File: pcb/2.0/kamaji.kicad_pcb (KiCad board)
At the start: 2 copper layers, 100 x 100 mm, 92 parts, among them J1 RJ10, J2 RJ10, J3 RJ10, J4 RJ10, J5 RJ10, J6 RJ10, J7 USB_B, J8 USB_A, Q1 2N3904, Q2 IRL540N, Q3 IRL540N, SW1 SW_Push, SW2 SW_Push, SW3 SW_Push, U1 ATMEGA32U4-AU, Y1 16MHz

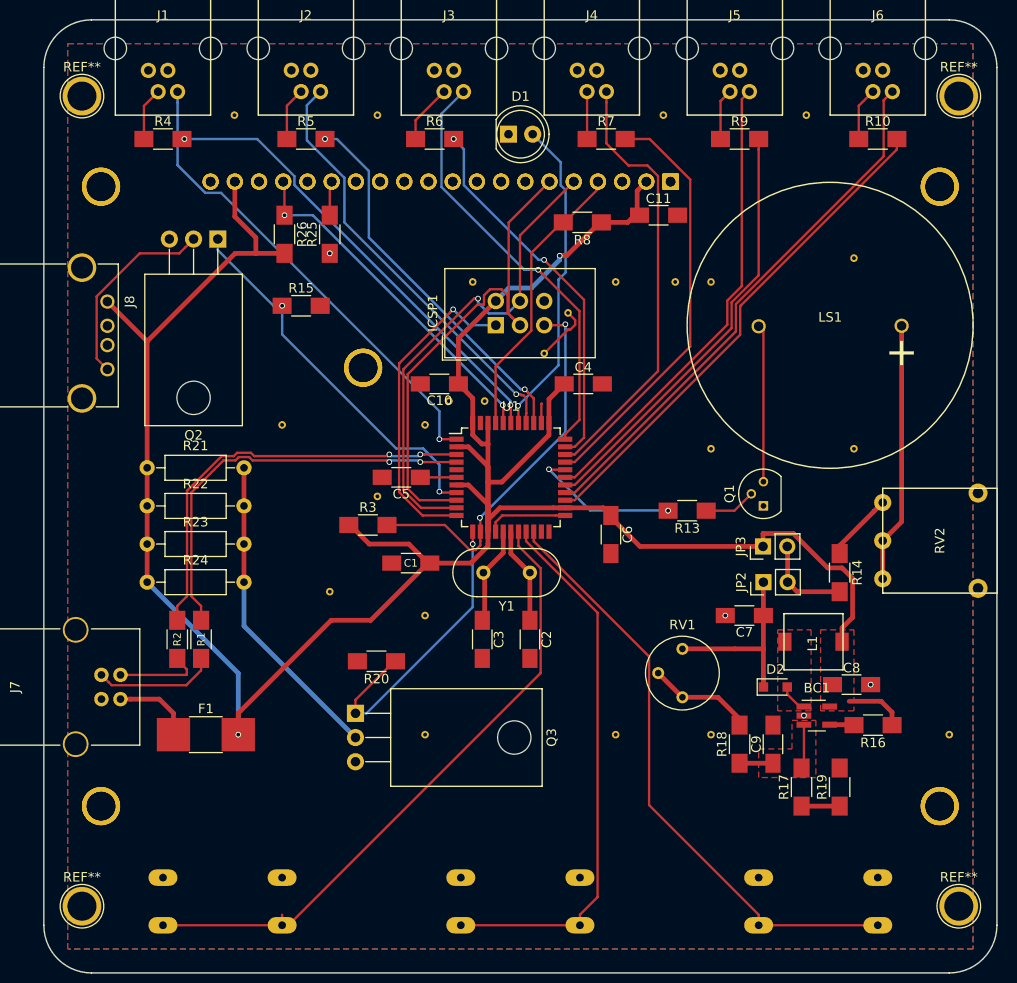
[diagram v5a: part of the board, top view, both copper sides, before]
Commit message: silkscreen text
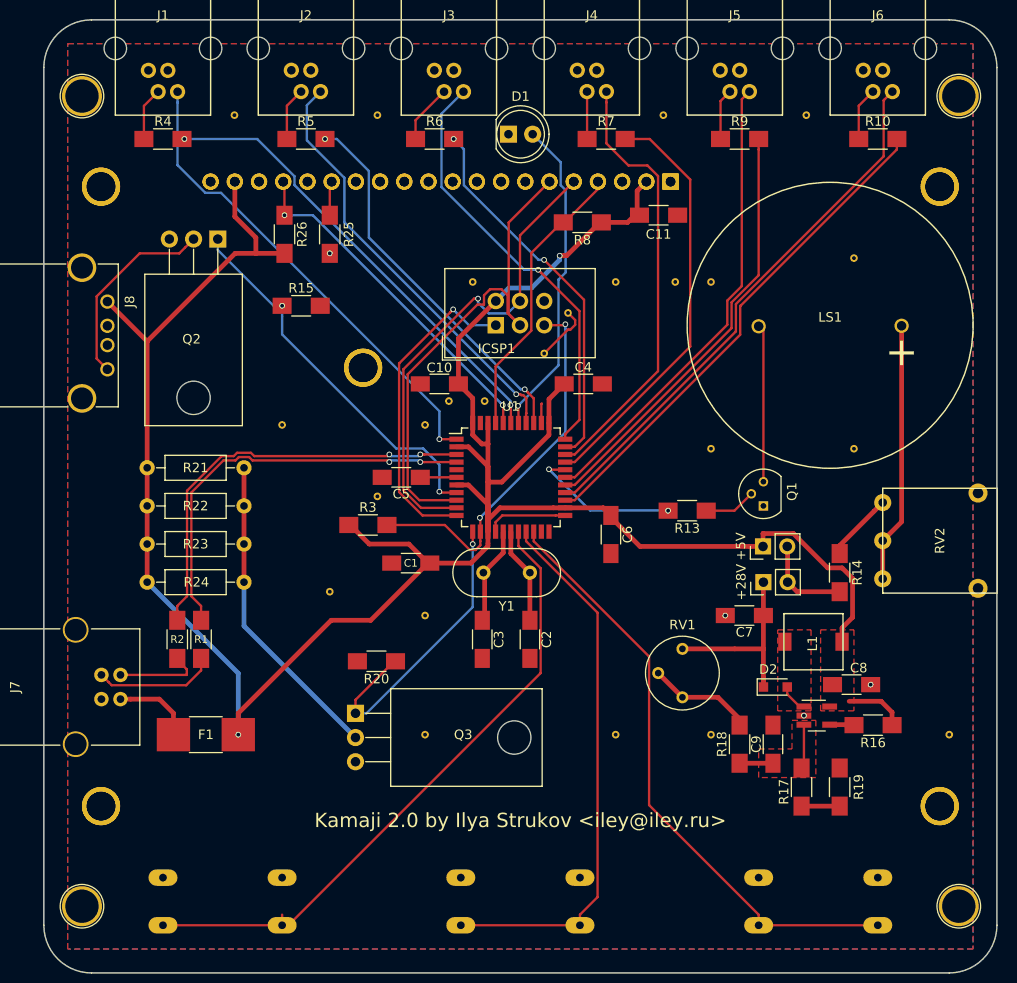
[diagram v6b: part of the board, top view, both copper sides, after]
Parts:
- renumbered JP2 to +28V, JP3 to +5V
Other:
- board text added: "Kamaji 2.0 by Ilya Strukov <iley@iley.ru>"
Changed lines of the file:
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@@
 (kicad_pcb (version 4) (host pcbnew 4.0.7)
   (general
-    (links 0)
+    (links 203)
     (no_connects 1)
     (area 49.924999 49.924999 150.075001 150.075001)
     (thickness 1.6)
-    (drawings 8)
+    (drawings 9)
     (tracks 450)
     (zones 0)
@@
     (mod_text_size 1 1)
     (mod_text_width 0.15)
-    (pad_size 4.064 4.064)
-    (pad_drill 3.048)
+    (pad_size 4.2 4.2)
+    (pad_drill 3.5)
     (pad_to_mask_clearance 0.2)
     (aux_axis_origin 0 0)
@@
     (descr "module 1 pin (ou trou mecanique de percage)")
     (tags DEV)
-    (fp_text reference REF** (at 0 -3.048) (layer F.SilkS)
+    (fp_text reference REF** (at 0 -3.048) (layer F.SilkS) hide
       (effects (font (size 1 1) (thickness 0.15)))
     )
@@
     (fp_circle (center 0 0) (end 2.6 0) (layer F.CrtYd) (width 0.05))
     (fp_circle (center 0 0) (end 0 -2.286) (layer F.SilkS) (width 0.12))
-    (pad "" np_thru_hole circle (at 0 0) (size 4.064 4.064) (drill 3.048) (layers *.Cu *.Mask))
+    (pad "" np_thru_hole circle (at 0 0) (size 4.2 4.2) (drill 3.5) (layers *.Cu *.Mask))
   )
   (module Connectors:1pin (layer F.Cu)
@@
     (descr "module 1 pin (ou trou mecanique de percage)")
     (tags DEV)
-    (fp_text reference REF** (at 0 -3.048) (layer F.SilkS)
+    (fp_text reference REF** (at 0 -3.048) (layer F.SilkS) hide
       (effects (font (size 1 1) (thickness 0.15)))
     )
@@
     (fp_circle (center 0 0) (end 2.6 0) (layer F.CrtYd) (width 0.05))
     (fp_circle (center 0 0) (end 0 -2.286) (layer F.SilkS) (width 0.12))
-    (pad "" np_thru_hole circle (at 0 0) (size 4.064 4.064) (drill 3.048) (layers *.Cu *.Mask))
+    (pad "" np_thru_hole circle (at 0 0) (size 4.2 4.2) (drill 3.5) (layers *.Cu *.Mask))
   )
   (module Connectors:1pin (layer F.Cu)
@@
     (descr "module 1 pin (ou trou mecanique de percage)")
     (tags DEV)
-    (fp_text reference REF** (at 0 -3.048) (layer F.SilkS)
+    (fp_text reference REF** (at 0 -3.048) (layer F.SilkS) hide
       (effects (font (size 1 1) (thickness 0.15)))
     )
@@
     (fp_circle (center 0 0) (end 2.6 0) (layer F.CrtYd) (width 0.05))
     (fp_circle (center 0 0) (end 0 -2.286) (layer F.SilkS) (width 0.12))
-    (pad "" np_thru_hole circle (at 0 0) (size 4.064 4.064) (drill 3.048) (layers *.Cu *.Mask))
+    (pad "" np_thru_hole circle (at 0 0) (size 4.2 4.2) (drill 3.5) (layers *.Cu *.Mask))
   )
   (module kamaji:Via_0.8mm (layer F.Cu)
@@
     (descr "TO-220-3, Horizontal, RM 2.54mm")
     (tags "TO-220-3 Horizontal RM 2.54mm")
-    (fp_text reference Q3 (at 2.54 -20.58 270) (layer F.SilkS)
+    (fp_text reference Q3 (at 2.24 -11.3 360) (layer F.SilkS)
       (effects (font (size 1 1) (thickness 0.15)))
     )
@@
     (descr "TO-92 leads molded, narrow, drill 0.6mm (see NXP sot054_po.pdf)")
     (tags "to-92 sc-43 sc-43a sot54 PA33 transistor")
-    (fp_text reference Q1 (at 1.27 -3.56 90) (layer F.SilkS)
+    (fp_text reference Q1 (at 1.5 3 90) (layer F.SilkS)
       (effects (font (size 1 1) (thickness 0.15)))
     )
@@
     (descr "6 pins through hole IDC header")
     (tags "IDC header socket VASCH AVR ISP")
-    (fp_text reference ICSP1 (at 1.27 -6.604 90) (layer F.SilkS)
+    (fp_text reference ICSP1 (at -2.46 0.08 180) (layer F.SilkS)
       (effects (font (size 1 1) (thickness 0.15)))
     )
@@
     (tags "SOT-23-5 hand-soldering")
     (attr smd)
-    (fp_text reference BC1 (at 0 -2.9) (layer F.SilkS)
+    (fp_text reference BC1 (at 0 -2.9) (layer F.SilkS) hide
       (effects (font (size 1 1) (thickness 0.15)))
     )
@@
     (tags "capacitor 1206")
     (attr smd)
-    (fp_text reference C8 (at 0 -1.75) (layer F.SilkS)
+    (fp_text reference C8 (at 0.75 -1.75) (layer F.SilkS)
       (effects (font (size 1 1) (thickness 0.15)))
     )
@@
     (tags "capacitor 1206")
     (attr smd)
-    (fp_text reference C10 (at 0 -1.75 180) (layer F.SilkS)
+    (fp_text reference C10 (at 0 1.7 360) (layer F.SilkS)
       (effects (font (size 1 1) (thickness 0.15)))
     )
@@
     (tags SOD-323)
     (attr smd)
-    (fp_text reference D2 (at 0 -1.85) (layer F.SilkS)
+    (fp_text reference D2 (at -0.75 -1.85) (layer F.SilkS)
       (effects (font (size 1 1) (thickness 0.15)))
     )
@@
     (tags "resistor 1812")
     (attr smd)
-    (fp_text reference F1 (at 0 -2.72) (layer F.SilkS)
+    (fp_text reference F1 (at 0 0) (layer F.SilkS)
       (effects (font (size 1 1) (thickness 0.15)))
     )
@@
     (descr "Through hole straight socket strip, 1x02, 2.54mm pitch, single row")
     (tags "Through hole socket strip THT 1x02 2.54mm single row")
-    (fp_text reference JP2 (at 0 -2.33 90) (layer F.SilkS)
+    (fp_text reference +28V (at 0 -2.33 90) (layer F.SilkS)
       (effects (font (size 1 1) (thickness 0.15)))
     )
@@
     (descr "Through hole straight socket strip, 1x02, 2.54mm pitch, single row")
     (tags "Through hole socket strip THT 1x02 2.54mm single row")
-    (fp_text reference JP3 (at 0 -2.33 90) (layer F.SilkS)
+    (fp_text reference +5V (at 0 -2.33 90) (layer F.SilkS)
       (effects (font (size 1 1) (thickness 0.15)))
     )
@@
     (descr "TO-220-3, Horizontal, RM 2.54mm")
     (tags "TO-220-3 Horizontal RM 2.54mm")
-    (fp_text reference Q2 (at 2.54 -20.58 180) (layer F.SilkS)
+    (fp_text reference Q2 (at 2.75 -10.5 180) (layer F.SilkS)
       (effects (font (size 1 1) (thickness 0.15)))
     )
@@
     (tags "resistor 1206")
     (attr smd)
-    (fp_text reference R1 (at 0 0 270) (layer F.SilkS)
+    (fp_text reference R1 (at 0 0 360) (layer F.SilkS)
       (effects (font (size 0.8 0.8) (thickness 0.15)))
     )
@@
     (tags "resistor 1206")
     (attr smd)
-    (fp_text reference R2 (at 0 0 270) (layer F.SilkS)
+    (fp_text reference R2 (at 0 0 360) (layer F.SilkS)
       (effects (font (size 0.8 0.8) (thickness 0.15)))
     )
@@
     (tags "resistor 1206")
     (attr smd)
-    (fp_text reference R17 (at 0 -1.85 90) (layer F.SilkS)
+    (fp_text reference R17 (at -0.5 -1.85 90) (layer F.SilkS)
       (effects (font (size 1 1) (thickness 0.15)))
     )
@@
     (tags "resistor 1206")
     (attr smd)
-    (fp_text reference R19 (at 0 -1.85 90) (layer F.SilkS)
+    (fp_text reference R19 (at 0 2 90) (layer F.SilkS)
       (effects (font (size 1 1) (thickness 0.15)))
     )
@@
     (tags "resistor 1206")
     (attr smd)
-    (fp_text reference R25 (at 0 -1.85 90) (layer F.SilkS)
+    (fp_text reference R25 (at 0 2 90) (layer F.SilkS)
       (effects (font (size 1 1) (thickness 0.15)))
     )
@@
     (descr "Resistor, Axial_DIN0207 series, Axial, Horizontal, pin pitch=10.16mm, 0.25W = 1/4W, length*diameter=6.3*2.5mm^2, http://cdn-reichelt.de/documents/datenblatt/B400/1_4W%23YAG.pdf")
     (tags "Resistor Axial_DIN0207 series Axial Horizontal pin pitch 10.16mm 0.25W = 1/4W length 6.3mm diameter 2.5mm")
-    (fp_text reference R21 (at 5.08 -2.31) (layer F.SilkS)
+    (fp_text reference R21 (at 5.08 0) (layer F.SilkS)
       (effects (font (size 1 1) (thickness 0.15)))
     )
@@
     (descr "Resistor, Axial_DIN0207 series, Axial, Horizontal, pin pitch=10.16mm, 0.25W = 1/4W, length*diameter=6.3*2.5mm^2, http://cdn-reichelt.de/documents/datenblatt/B400/1_4W%23YAG.pdf")
     (tags "Resistor Axial_DIN0207 series Axial Horizontal pin pitch 10.16mm 0.25W = 1/4W length 6.3mm diameter 2.5mm")
-    (fp_text reference R22 (at 5.08 -2.31) (layer F.SilkS)
+    (fp_text reference R22 (at 5.08 0) (layer F.SilkS)
       (effects (font (size 1 1) (thickness 0.15)))
     )
@@
     (descr "Resistor, Axial_DIN0207 series, Axial, Horizontal, pin pitch=10.16mm, 0.25W = 1/4W, length*diameter=6.3*2.5mm^2, http://cdn-reichelt.de/documents/datenblatt/B400/1_4W%23YAG.pdf")
     (tags "Resistor Axial_DIN0207 series Axial Horizontal pin pitch 10.16mm 0.25W = 1/4W length 6.3mm diameter 2.5mm")
-    (fp_text reference R23 (at 5.08 -2.31) (layer F.SilkS)
+    (fp_text reference R23 (at 5.08 0) (layer F.SilkS)
       (effects (font (size 1 1) (thickness 0.15)))
     )
@@
     (descr "Resistor, Axial_DIN0207 series, Axial, Horizontal, pin pitch=10.16mm, 0.25W = 1/4W, length*diameter=6.3*2.5mm^2, http://cdn-reichelt.de/documents/datenblatt/B400/1_4W%23YAG.pdf")
     (tags "Resistor Axial_DIN0207 series Axial Horizontal pin pitch 10.16mm 0.25W = 1/4W length 6.3mm diameter 2.5mm")
-    (fp_text reference R24 (at 5.08 -2.31) (layer F.SilkS)
+    (fp_text reference R24 (at 5.16 0) (layer F.SilkS)
       (effects (font (size 1 1) (thickness 0.15)))
     )
@@
     (tags "capacitor 1206")
     (attr smd)
-    (fp_text reference C11 (at 0 -1.75) (layer F.SilkS)
+    (fp_text reference C11 (at 0 2) (layer F.SilkS)
       (effects (font (size 1 1) (thickness 0.15)))
     )
@@
     (descr "module 1 pin (ou trou mecanique de percage)")
     (tags DEV)
-    (fp_text reference REF** (at 0 -3.048) (layer F.SilkS)
+    (fp_text reference REF** (at 0 -3.048) (layer F.SilkS) hide
       (effects (font (size 1 1) (thickness 0.15)))
     )
@@
     (fp_circle (center 0 0) (end 2.6 0) (layer F.CrtYd) (width 0.05))
     (fp_circle (center 0 0) (end 0 -2.286) (layer F.SilkS) (width 0.12))
-    (pad "" np_thru_hole circle (at 0 0) (size 4.064 4.064) (drill 3.048) (layers *.Cu *.Mask))
+    (pad "" np_thru_hole circle (at 0 0) (size 4.2 4.2) (drill 3.5) (layers *.Cu *.Mask))
+  )
+  (gr_text "Kamaji 2.0 by Ilya Strukov <iley@iley.ru>" (at 100 134) (layer F.SilkS)
+    (effects (font (size 1.5 1.5) (thickness 0.25)))
   )
   (gr_line (start 50 145) (end 50 55) (layer Edge.Cuts) (width 0.15))

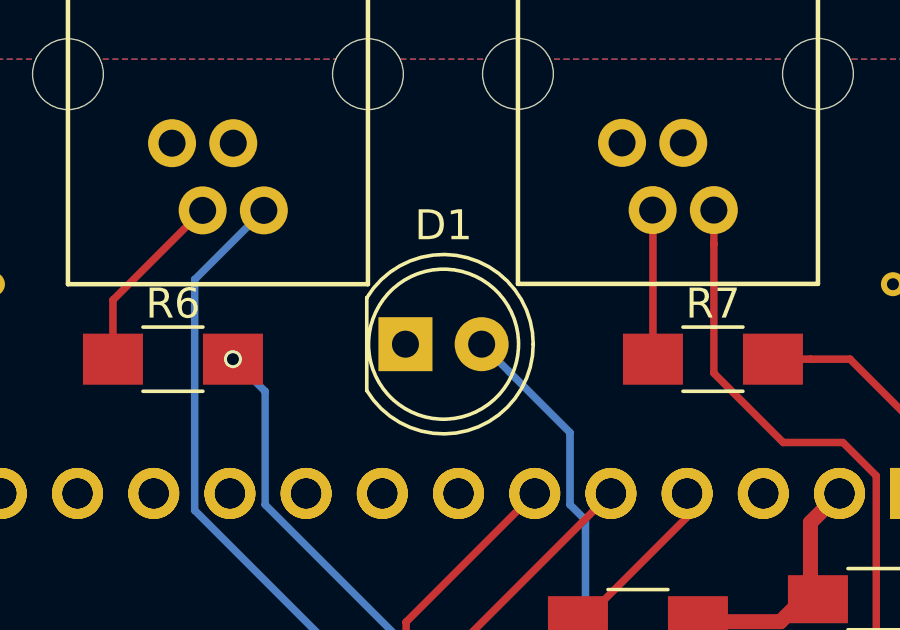
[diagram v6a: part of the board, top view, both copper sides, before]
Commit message: flip the signal LED
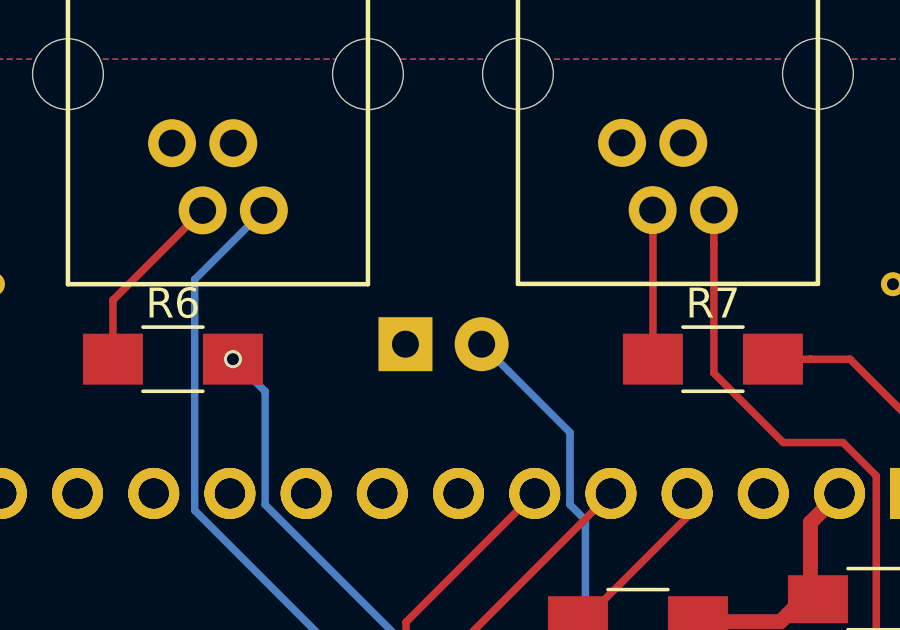
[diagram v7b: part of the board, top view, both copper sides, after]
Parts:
- D1: moved to B.Cu
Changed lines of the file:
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@@
     (links 203)
     (no_connects 1)
-    (area 49.924999 49.924999 150.075001 150.075001)
+    (area 42.564999 46.54 152.093 150.075001)
     (thickness 1.6)
     (drawings 9)
@@
     )
   )
-  (module LEDs:LED_D5.0mm (layer F.Cu)
+  (module LEDs:LED_D5.0mm (layer B.Cu)
     (at 98.75 62)
     (descr "LED, diameter 5.0mm, 2 pins, http://cdn-reichelt.de/documents/datenblatt/A500/LL-504BC2E-009.pdf")
     (tags "LED diameter 5.0mm 2 pins")
-    (fp_text reference D1 (at 1.27 -3.96) (layer F.SilkS)
-      (effects (font (size 1 1) (thickness 0.15)))
-    )
-    (fp_text value LED (at 1.27 3.96) (layer F.Fab)
-      (effects (font (size 1 1) (thickness 0.15)))
-    )
-    (fp_arc (start 1.27 0) (end -1.23 -1.469694) (angle 299.1) (layer F.Fab) (width 0.1))
-    (fp_arc (start 1.27 0) (end -1.29 -1.54483) (angle 148.9) (layer F.SilkS) (width 0.12))
-    (fp_arc (start 1.27 0) (end -1.29 1.54483) (angle -148.9) (layer F.SilkS) (width 0.12))
-    (fp_circle (center 1.27 0) (end 3.77 0) (layer F.Fab) (width 0.1))
-    (fp_circle (center 1.27 0) (end 3.77 0) (layer F.SilkS) (width 0.12))
-    (fp_line (start -1.23 -1.469694) (end -1.23 1.469694) (layer F.Fab) (width 0.1))
-    (fp_line (start -1.29 -1.545) (end -1.29 1.545) (layer F.SilkS) (width 0.12))
-    (fp_line (start -1.95 -3.25) (end -1.95 3.25) (layer F.CrtYd) (width 0.05))
-    (fp_line (start -1.95 3.25) (end 4.5 3.25) (layer F.CrtYd) (width 0.05))
-    (fp_line (start 4.5 3.25) (end 4.5 -3.25) (layer F.CrtYd) (width 0.05))
-    (fp_line (start 4.5 -3.25) (end -1.95 -3.25) (layer F.CrtYd) (width 0.05))
-    (fp_text user %R (at 1.25 0) (layer F.Fab)
-      (effects (font (size 0.8 0.8) (thickness 0.2)))
+    (fp_text reference D1 (at -2.5 0) (layer B.SilkS)
+      (effects (font (size 1 1) (thickness 0.15)) (justify mirror))
+    )
+    (fp_text value LED (at 1.27 -3.96) (layer B.Fab)
+      (effects (font (size 1 1) (thickness 0.15)) (justify mirror))
+    )
+    (fp_arc (start 1.27 0) (end -1.23 1.469694) (angle -299.1) (layer B.Fab) (width 0.1))
+    (fp_arc (start 1.27 0) (end -1.29 1.54483) (angle -148.9) (layer B.SilkS) (width 0.12))
+    (fp_arc (start 1.27 0) (end -1.29 -1.54483) (angle 148.9) (layer B.SilkS) (width 0.12))
+    (fp_circle (center 1.27 0) (end 3.77 0) (layer B.Fab) (width 0.1))
+    (fp_circle (center 1.27 0) (end 3.77 0) (layer B.SilkS) (width 0.12))
+    (fp_line (start -1.23 1.469694) (end -1.23 -1.469694) (layer B.Fab) (width 0.1))
+    (fp_line (start -1.29 1.545) (end -1.29 -1.545) (layer B.SilkS) (width 0.12))
+    (fp_line (start -1.95 3.25) (end -1.95 -3.25) (layer B.CrtYd) (width 0.05))
+    (fp_line (start -1.95 -3.25) (end 4.5 -3.25) (layer B.CrtYd) (width 0.05))
+    (fp_line (start 4.5 -3.25) (end 4.5 3.25) (layer B.CrtYd) (width 0.05))
+    (fp_line (start 4.5 3.25) (end -1.95 3.25) (layer B.CrtYd) (width 0.05))
+    (fp_text user %R (at 1.25 0) (layer B.Fab)
+      (effects (font (size 0.8 0.8) (thickness 0.2)) (justify mirror))
     )
     (pad 1 thru_hole rect (at 0 0) (size 1.8 1.8) (drill 0.9) (layers *.Cu *.Mask)
